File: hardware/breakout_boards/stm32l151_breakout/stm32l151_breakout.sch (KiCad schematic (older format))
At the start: 12 parts, among them J1 USB_B_Micro, J2 Conn_01x24_Male, J3 Conn_ARM_JTAG_SWD_10, J4 Conn_01x24_Male, U1 LD1117-3.3, U2 STM32L151C

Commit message: Finish out initial board
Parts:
- added D1: LED, symbol device:LED
- added R1: 40, symbol device:R
- 0.1uF4: value C3 -> C4
- 0.1uF5: value C4 -> C5
- 10uF1: value C5 -> C6
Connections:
- net +3.3V: now also D1.2 (A)
- net GND: now also R1.2
- new net: D1.1 (K), R1.1
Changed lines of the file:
@@
 P 5250 6750
 F 0 "0.1uF4" H 5365 6796 50  0000 L CNN
-F 1 "C3" H 5365 6705 50  0000 L CNN
+F 1 "C4" H 5365 6705 50  0000 L CNN
 F 2 "Capacitors_SMD:C_0805_HandSoldering" H 5288 6600 50  0001 C CNN
 F 3 "" H 5250 6750 50  0001 C CNN
@@
 P 6000 6750
 F 0 "0.1uF5" H 6115 6796 50  0000 L CNN
-F 1 "C4" H 6115 6705 50  0000 L CNN
+F 1 "C5" H 6115 6705 50  0000 L CNN
 F 2 "Capacitors_SMD:C_0805_HandSoldering" H 6038 6600 50  0001 C CNN
 F 3 "" H 6000 6750 50  0001 C CNN
@@
 P 6500 6750
 F 0 "10uF1" H 6615 6796 50  0000 L CNN
-F 1 "C5" H 6615 6705 50  0000 L CNN
+F 1 "C6" H 6615 6705 50  0000 L CNN
 F 2 "Capacitors_SMD:C_0805_HandSoldering" H 6538 6600 50  0001 C CNN
 F 3 "" H 6500 6750 50  0001 C CNN
@@
 	1    0    0    -1
 $EndComp
+$Comp
+L device:LED D1
+U 1 1 5A327D93
+P 2650 6700
+F 0 "D1" V 2688 6583 50  0000 R CNN
+F 1 "LED" V 2597 6583 50  0000 R CNN
+F 2 "" H 2650 6700 50  0001 C CNN
+F 3 "~" H 2650 6700 50  0001 C CNN
+	1    2650 6700
+	0    -1   -1   0
+$EndComp
+Wire Wire Line
+	2650 6350 2650 6550
+Connection ~ 2650 6350
+$Comp
+L power:GND #PWR?
+U 1 1 5A33D07D
+P 2650 7250
+F 0 "#PWR?" H 2650 7000 50  0001 C CNN
+F 1 "GND" H 2655 7077 50  0000 C CNN
+F 2 "" H 2650 7250 50  0001 C CNN
+F 3 "" H 2650 7250 50  0001 C CNN
+	1    2650 7250
+	1    0    0    -1
+$EndComp
+$Comp
+L device:R R1
+U 1 1 5A33DA6A
+P 2650 7050
+F 0 "R1" H 2720 7096 50  0000 L CNN
+F 1 "40" H 2720 7005 50  0000 L CNN
+F 2 "" V 2580 7050 50  0001 C CNN
+F 3 "" H 2650 7050 50  0001 C CNN
+	1    2650 7050
+	1    0    0    -1
+$EndComp
+Wire Wire Line
+	2650 6850 2650 6900
+Wire Wire Line
+	2650 7200 2650 7250
 $EndSCHEMATC

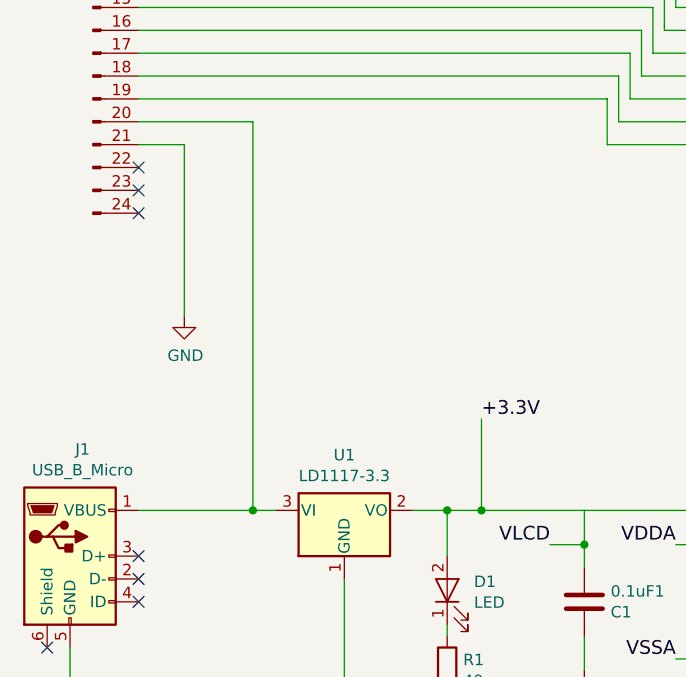
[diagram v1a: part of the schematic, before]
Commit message: Add breakout board pin labels
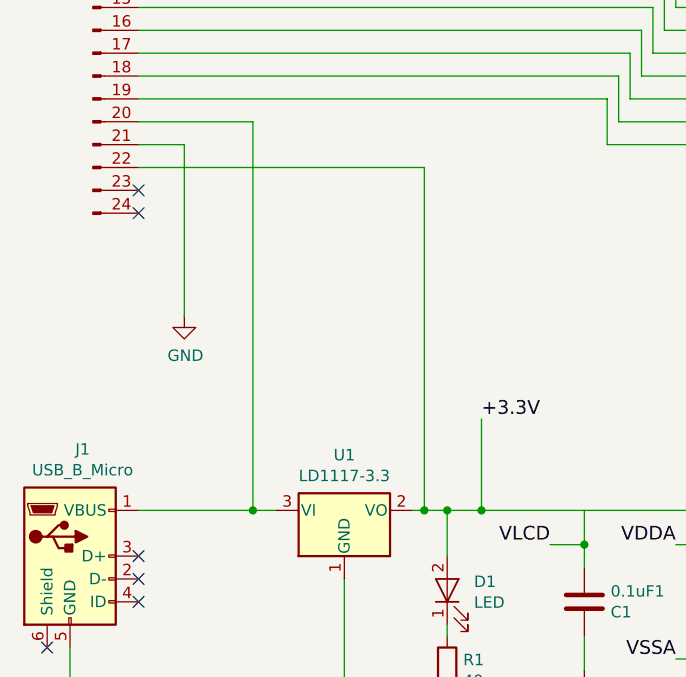
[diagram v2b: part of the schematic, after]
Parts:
- D1: footprint (none) -> LEDs:LED_0805_HandSoldering
- R1: footprint (none) -> Resistors_SMD:R_0805_HandSoldering
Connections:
- net +3.3V: now also J2.22 (Pin_22)
- no-connect marks 10 -> 9
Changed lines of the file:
@@
 	1    0    0    -1
 $EndComp
-NoConn ~ 1300 4850
 NoConn ~ 1300 4950
 NoConn ~ 1300 5050
@@
 F 0 "D1" V 2688 6583 50  0000 R CNN
 F 1 "LED" V 2597 6583 50  0000 R CNN
-F 2 "" H 2650 6700 50  0001 C CNN
+F 2 "LEDs:LED_0805_HandSoldering" H 2650 6700 50  0001 C CNN
 F 3 "~" H 2650 6700 50  0001 C CNN
 	1    2650 6700
@@
 Connection ~ 2650 6350
 $Comp
-L power:GND #PWR?
+L power:GND #PWR012
 U 1 1 5A33D07D
 P 2650 7250
-F 0 "#PWR?" H 2650 7000 50  0001 C CNN
+F 0 "#PWR012" H 2650 7000 50  0001 C CNN
 F 1 "GND" H 2655 7077 50  0000 C CNN
 F 2 "" H 2650 7250 50  0001 C CNN
@@
 F 0 "R1" H 2720 7096 50  0000 L CNN
 F 1 "40" H 2720 7005 50  0000 L CNN
-F 2 "" V 2580 7050 50  0001 C CNN
+F 2 "Resistors_SMD:R_0805_HandSoldering" V 2580 7050 50  0001 C CNN
 F 3 "" H 2650 7050 50  0001 C CNN
 	1    2650 7050
@@
 Wire Wire Line
 	2650 7200 2650 7250
+Wire Wire Line
+	1300 4850 2550 4850
+Wire Wire Line
+	2550 4850 2550 6350
+Connection ~ 2550 6350
 $EndSCHEMATC

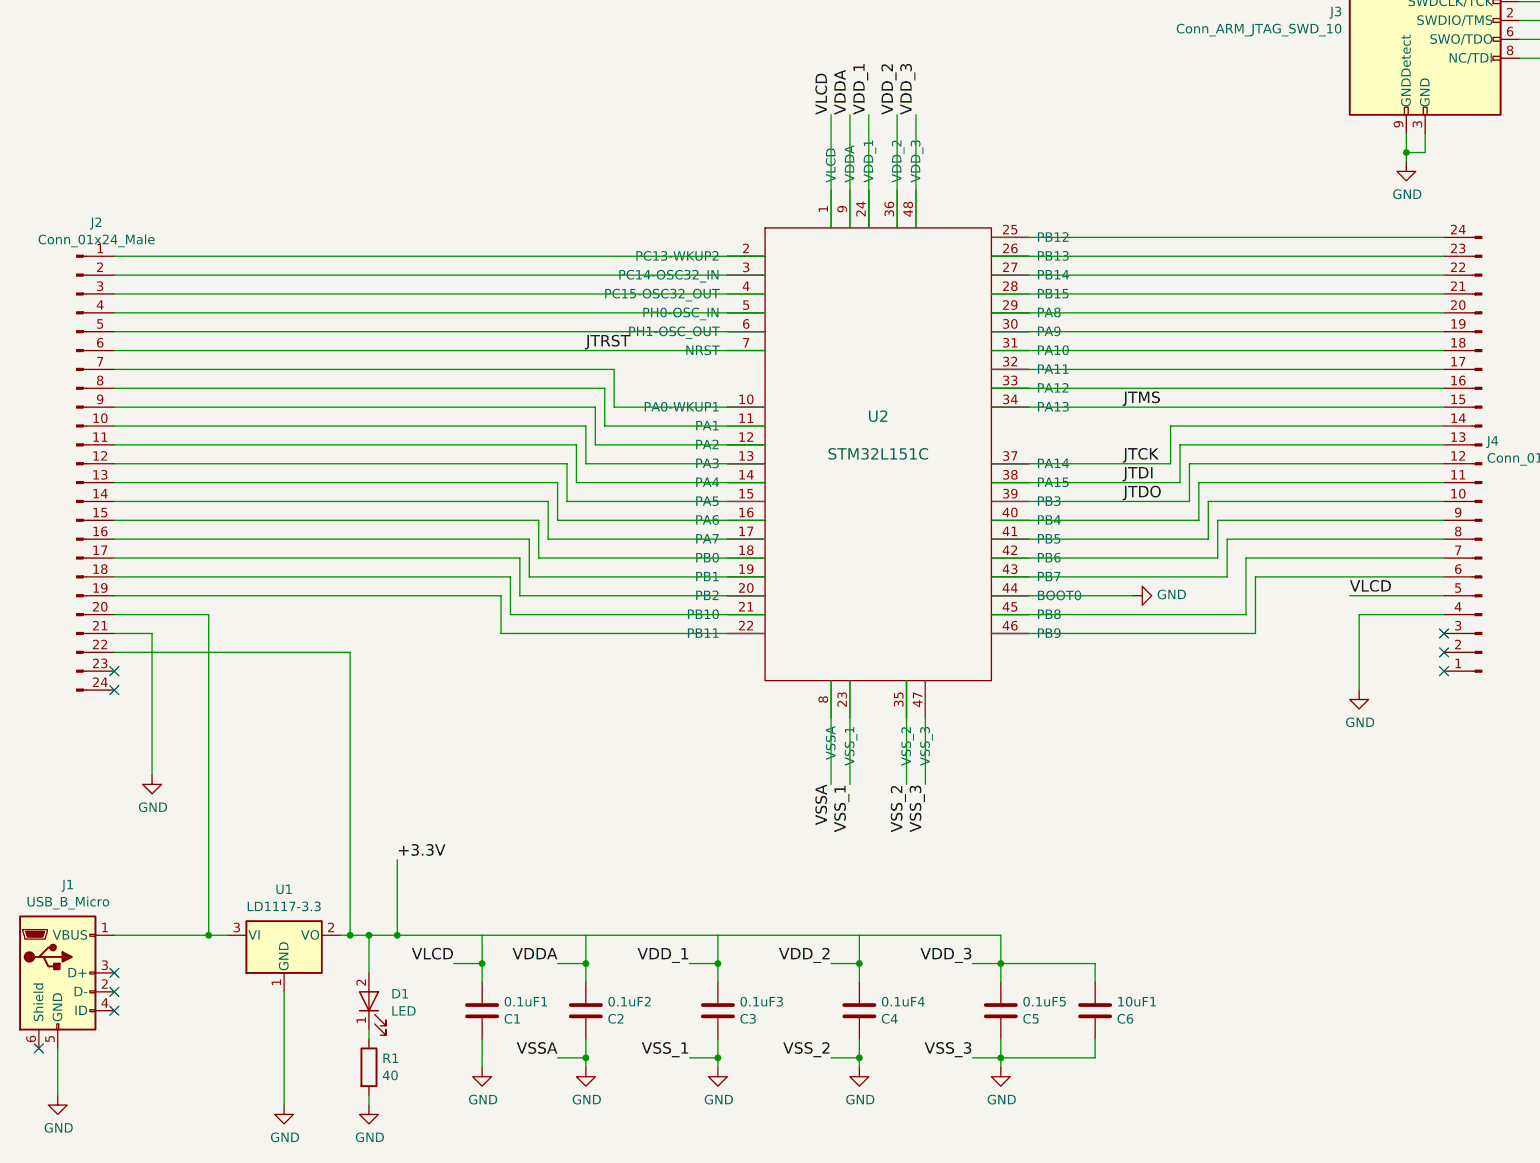
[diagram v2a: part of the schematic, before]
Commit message: Update stm32l breakout board to use a 1.27mm jtag connector
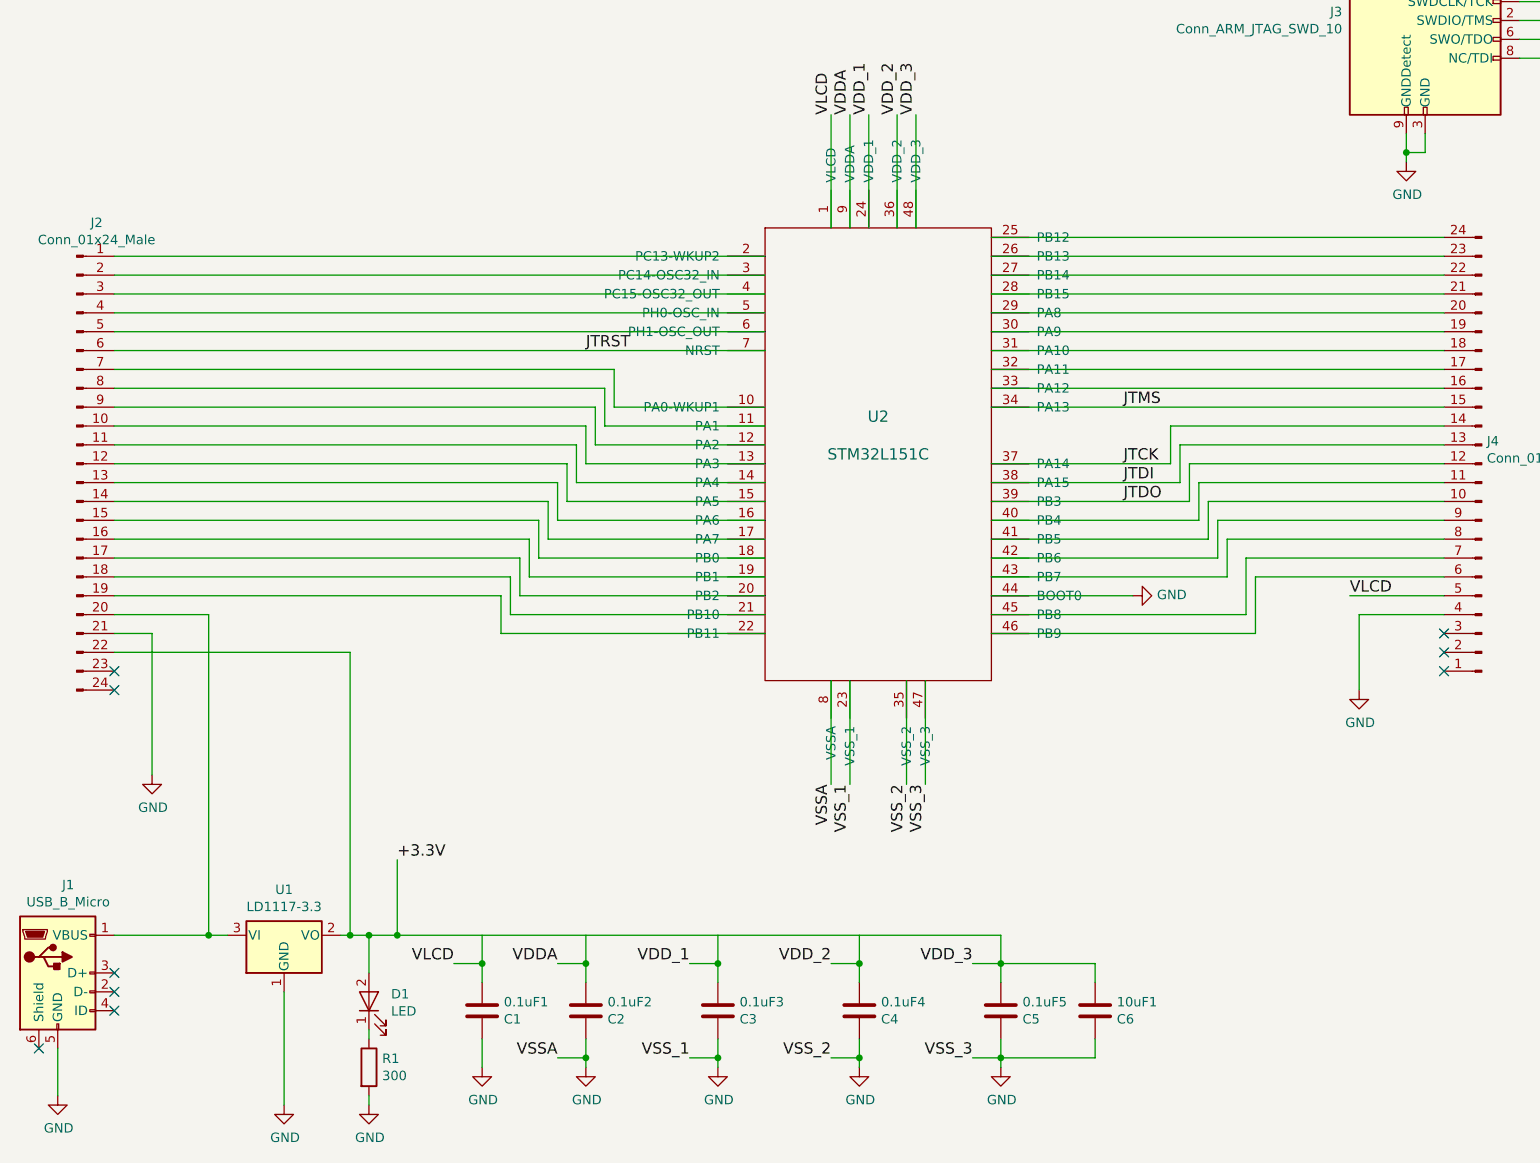
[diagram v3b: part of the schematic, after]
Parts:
- J3: footprint Pin_Headers:Pin_Header_Straight_2x05_Pitch2.54mm -> Pin_Headers:Pin_Header_Straight_2x05_Pitch1.27mm
- R1: value 40 -> 300
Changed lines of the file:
@@
 F 0 "J3" H 7810 1546 50  0000 R CNN
 F 1 "Conn_ARM_JTAG_SWD_10" H 7810 1455 50  0000 R CNN
-F 2 "Pin_Headers:Pin_Header_Straight_2x05_Pitch2.54mm" H 8300 950 50  0001 L TNN
+F 2 "Pin_Headers:Pin_Header_Straight_2x05_Pitch1.27mm" H 8300 950 50  0001 L TNN
 F 3 "http://infocenter.arm.com/help/topic/com.arm.doc.faqs/attached/13634/cortex_debug_connectors.pdf" V 7900 250 50  0001 C CNN
 	1    8250 1500
@@
 	5950 3950 6950 3950
 Wire Wire Line
-	8150 2100 8150 2250
+	8150 2100 8150 2200
 Wire Wire Line
 	8250 2200 8150 2200
@@
 	1000 6950 1000 7200
 Wire Wire Line
-	3800 6600 3800 6350
-Wire Wire Line
-	3800 6900 3800 7050
+	3800 6600 3800 6500
+Wire Wire Line
+	3800 6900 3800 7000
 Wire Wire Line
 	3800 6500 3650 6500
@@
 Connection ~ 3800 7000
 Wire Wire Line
-	4500 6600 4500 6350
-Wire Wire Line
-	4500 6900 4500 7050
+	4500 6600 4500 6500
+Wire Wire Line
+	4500 6900 4500 7000
 Wire Wire Line
 	4500 6500 4350 6500
@@
 Connection ~ 4500 7000
 Wire Wire Line
-	5250 6600 5250 6350
-Wire Wire Line
-	5250 6900 5250 7050
+	5250 6600 5250 6500
+Wire Wire Line
+	5250 6900 5250 7000
 Wire Wire Line
 	5250 6500 5100 6500
@@
 Connection ~ 5250 7000
 Wire Wire Line
-	6000 6600 6000 6350
-Wire Wire Line
-	6000 6900 6000 7050
-Wire Wire Line
-	5850 6500 6500 6500
+	6000 6600 6000 6500
+Wire Wire Line
+	6000 6900 6000 7000
+Wire Wire Line
+	5850 6500 6000 6500
 Connection ~ 6000 6500
 Wire Wire Line
-	5850 7000 6500 7000
+	5850 7000 6000 7000
 Connection ~ 6000 7000
 Wire Wire Line
@@
 	6500 6900 6500 7000
 Wire Wire Line
-	1300 6350 1900 6350
-Wire Wire Line
-	2500 6350 6000 6350
+	1300 6350 1800 6350
+Wire Wire Line
+	2500 6350 2550 6350
 Wire Wire Line
 	2800 6350 2800 5950
@@
 VLCD
 Wire Wire Line
-	3250 6600 3250 6350
+	3250 6600 3250 6500
 Wire Wire Line
 	3250 6900 3250 7050
@@
 P 2650 7050
 F 0 "R1" H 2720 7096 50  0000 L CNN
-F 1 "40" H 2720 7005 50  0000 L CNN
+F 1 "300" H 2720 7005 50  0000 L CNN
 F 2 "Resistors_SMD:R_0805_HandSoldering" V 2580 7050 50  0001 C CNN
 F 3 "" H 2650 7050 50  0001 C CNN
@@
 	2550 4850 2550 6350
 Connection ~ 2550 6350
+Wire Wire Line
+	8150 2200 8150 2250
+Wire Wire Line
+	3800 6500 3800 6350
+Wire Wire Line
+	3800 7000 3800 7050
+Wire Wire Line
+	4500 6500 4500 6350
+Wire Wire Line
+	4500 7000 4500 7050
+Wire Wire Line
+	5250 6500 5250 6350
+Wire Wire Line
+	5250 7000 5250 7050
+Wire Wire Line
+	6000 6500 6000 6350
+Wire Wire Line
+	6000 6500 6500 6500
+Wire Wire Line
+	6000 7000 6000 7050
+Wire Wire Line
+	6000 7000 6500 7000
+Wire Wire Line
+	2800 6350 6000 6350
+Wire Wire Line
+	1800 6350 1900 6350
+Wire Wire Line
+	3250 6500 3250 6350
+Wire Wire Line
+	2650 6350 2800 6350
+Wire Wire Line
+	2550 6350 2650 6350
 $EndSCHEMATC

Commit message: Add updated as1115 breakout and stm32 breakout
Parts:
- removed J2, J4: Conn_01x24_Male, Pin_Headers:Pin_Header_Straight_2x12_Pitch2.54mm, symbol Connector:Conn_01x24_Male
- removed U2: STM32L151C, Housings_QFP:LQFP-48_7x7mm_Pitch0.5mm, symbol custom_ic:STM32L151C
- added C7: 0.1uF, symbol device:C
- added J?: Conn_01x24_Male, symbol Connector:Conn_01x24_Male
- added R2: 10K, symbol device:R
- added U2: STM32L151CCTx, Housings_QFP:LQFP-48_7x7mm_Pitch0.5mm, symbol MCU_ST_STM32:STM32L151CCTx
- C1: renamed from 0.1uF1; value C1 -> 0.1uF
- C2: renamed from 0.1uF2; value C2 -> 0.1uF
- C3: renamed from 0.1uF3; value C3 -> 0.1uF
- C4: renamed from 0.1uF4; value C4 -> 0.1uF
- C5: renamed from 0.1uF5; value C5 -> 0.1uF
- C6: renamed from 10uF1; value C6 -> 10uF
- renumbered J3 to J2
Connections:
- net labels added: +3V3, P1, P10, P11, P12, P13, P14, P15, P16, P17, P18, P19, P2, P20, P3, P4, P5, P6, P7, P8, P9
- net labels removed: VSSA, VSS_1, VSS_2, VSS_3
- wire segments 155 -> 93
- no-connect marks 9 -> 4
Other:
- moved on the sheet: C1, C2, C3, C4, C5, C6, D1, J1, J2, R1, U1
